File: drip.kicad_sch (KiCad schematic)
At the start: 96 parts, among them J1 ISP, J2 2xAA Battery Holder, Q1 2n2907, Q2 2n2907, Q3 2n2907, Q4 2n2907, Q5 2n2907, Q6 2n2907, Q7 2n2907, Q8 2n2907, Q9 2n2222, SW1 Bin, SW10 Recall, SW11 D, SW12 A, SW13 7, SW14 4, SW15 1, SW16 0, SW17 Hex, SW18 E, SW19 B, SW2 Store, SW20 8, SW21 5, SW22 2, SW23 Decimal, SW24 Oct, SW25 F, SW26 C, SW27 9, SW28 6, SW29 3, SW3 Shift, SW30 +/-, SW31 Clear, SW32 K, SW33 Div, SW34 Mul, SW35 Minus, SW36 Plus, SW37 Enter, SW4 1'sCompl, SW5 Or, SW6 And, SW7 Xor, SW8 Clear Entry, SW9 Dec, U1 74HC138, U2 5641AS-4Digit-7Segment, U3 5641AS-4Digit-7Segment, U4 MSP430G2553IN20, U5 74HC251, U6 74HC138, U7 74HC595, U8 XC6372A331PR-G

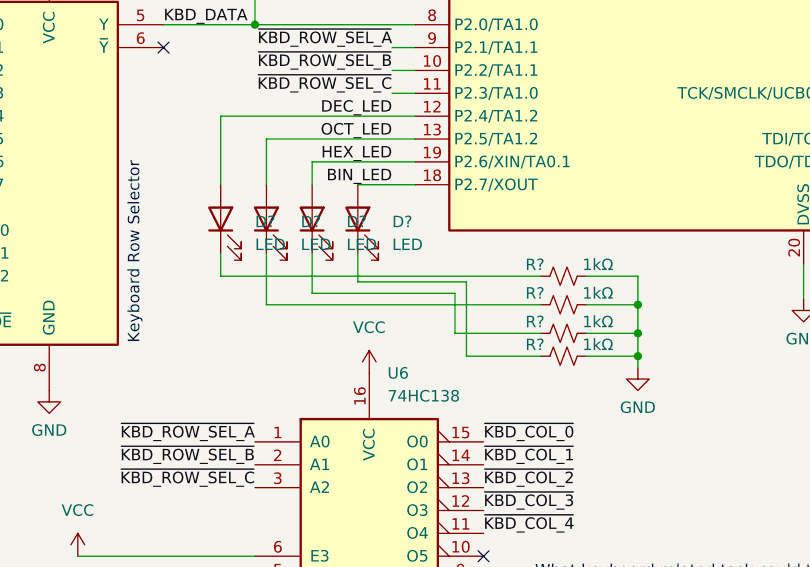
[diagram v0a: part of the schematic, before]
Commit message: Mode LEDs
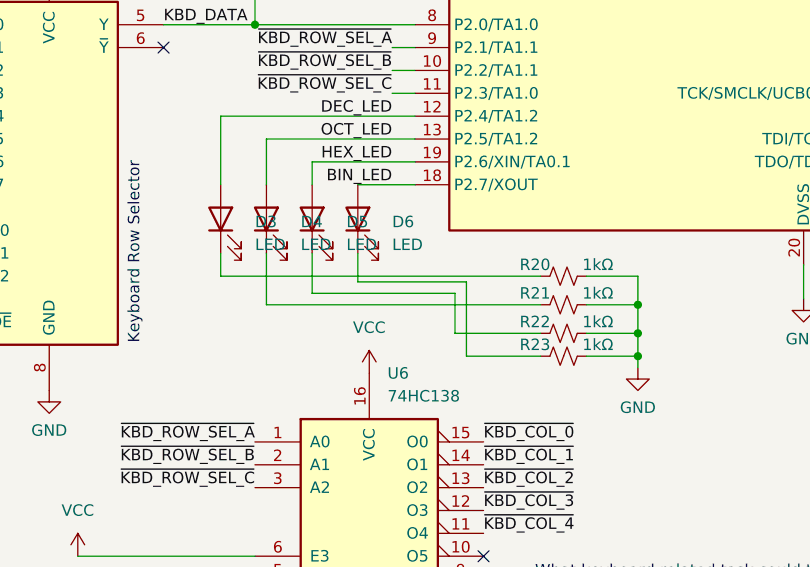
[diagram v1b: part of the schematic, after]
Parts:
- gave numbers to parts that had none: 8
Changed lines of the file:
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@@
   (symbol (lib_id "Device:LED") (at 135.89 203.835 90) (unit 1)
     (in_bom yes) (on_board yes) (fields_autoplaced)
-    (property "Reference" "D?" (id 0) (at 139.7 204.1524 90)
+    (property "Reference" "D4" (id 0) (at 139.7 204.1524 90)
       (effects (font (size 1.27 1.27)) (justify right))
     )
@@
   (symbol (lib_id "Device:R_Small_US") (at 168.91 216.535 90) (unit 1)
     (in_bom yes) (on_board yes)
-    (property "Reference" "R?" (id 0) (at 165.735 215.265 90))
+    (property "Reference" "R22" (id 0) (at 165.735 215.265 90))
     (property "Value" "1kΩ" (id 1) (at 172.72 215.265 90))
     (property "Footprint" "Resistor_SMD:R_0805_2012Metric_Pad1.20x1.40mm_HandSolder" (id 2) (at 168.91 216.535 0)
@@
   (symbol (lib_id "Device:LED") (at 140.97 203.835 90) (unit 1)
     (in_bom yes) (on_board yes) (fields_autoplaced)
-    (property "Reference" "D?" (id 0) (at 144.78 204.1524 90)
+    (property "Reference" "D5" (id 0) (at 144.78 204.1524 90)
       (effects (font (size 1.27 1.27)) (justify right))
     )
@@
   (symbol (lib_id "power:GND") (at 177.165 220.345 0) (unit 1)
     (in_bom yes) (on_board yes) (fields_autoplaced)
-    (property "Reference" "#PWR?" (id 0) (at 177.165 226.695 0)
+    (property "Reference" "#PWR0121" (id 0) (at 177.165 226.695 0)
       (effects (font (size 1.27 1.27)) hide)
     )
@@
   (symbol (lib_id "Device:R_Small_US") (at 168.91 219.075 90) (unit 1)
     (in_bom yes) (on_board yes)
-    (property "Reference" "R?" (id 0) (at 165.735 217.805 90))
+    (property "Reference" "R23" (id 0) (at 165.735 217.805 90))
     (property "Value" "1kΩ" (id 1) (at 172.72 217.805 90))
     (property "Footprint" "Resistor_SMD:R_0805_2012Metric_Pad1.20x1.40mm_HandSolder" (id 2) (at 168.91 219.075 0)
@@
   (symbol (lib_id "Device:LED") (at 146.05 203.835 90) (unit 1)
     (in_bom yes) (on_board yes) (fields_autoplaced)
-    (property "Reference" "D?" (id 0) (at 149.86 204.1524 90)
+    (property "Reference" "D6" (id 0) (at 149.86 204.1524 90)
       (effects (font (size 1.27 1.27)) (justify right))
     )
@@
   (symbol (lib_id "Device:R_Small_US") (at 168.91 210.185 90) (unit 1)
     (in_bom yes) (on_board yes)
-    (property "Reference" "R?" (id 0) (at 165.735 208.915 90))
+    (property "Reference" "R20" (id 0) (at 165.735 208.915 90))
     (property "Value" "1kΩ" (id 1) (at 172.72 208.915 90))
     (property "Footprint" "Resistor_SMD:R_0805_2012Metric_Pad1.20x1.40mm_HandSolder" (id 2) (at 168.91 210.185 0)
@@
   (symbol (lib_id "Device:LED") (at 130.81 203.835 90) (unit 1)
     (in_bom yes) (on_board yes) (fields_autoplaced)
-    (property "Reference" "D?" (id 0) (at 134.62 204.1524 90)
+    (property "Reference" "D3" (id 0) (at 134.62 204.1524 90)
       (effects (font (size 1.27 1.27)) (justify right))
     )
@@
   (symbol (lib_id "Device:R_Small_US") (at 168.91 213.36 90) (unit 1)
     (in_bom yes) (on_board yes)
-    (property "Reference" "R?" (id 0) (at 165.735 212.09 90))
+    (property "Reference" "R21" (id 0) (at 165.735 212.09 90))
     (property "Value" "1kΩ" (id 1) (at 172.72 212.09 90))
     (property "Footprint" "Resistor_SMD:R_0805_2012Metric_Pad1.20x1.40mm_HandSolder" (id 2) (at 168.91 213.36 0)
@@
     )
     (path "/673b1f10-dd13-4373-9e76-ed62eba7cac1"
-      (reference "#PWR?") (unit 1) (value "GND") (footprint "")
+      (reference "#PWR0121") (unit 1) (value "GND") (footprint "")
     )
     (path "/f2caa468-bb79-49cc-b0cf-a4c553ec891c"
@@
       (reference "D2") (unit 1) (value "1n5817") (footprint "Diode_THT:D_DO-41_SOD81_P10.16mm_Horizontal")
     )
+    (path "/be978f47-2533-42ed-ab73-ed75e74230d9"
+      (reference "D3") (unit 1) (value "LED") (footprint "LED_SMD:LED_0805_2012Metric_Pad1.15x1.40mm_HandSolder")
+    )
     (path "/22a290e3-58c4-4aae-b185-93fd6b844074"
-      (reference "D?") (unit 1) (value "LED") (footprint "LED_SMD:LED_0805_2012Metric_Pad1.15x1.40mm_HandSolder")
+      (reference "D4") (unit 1) (value "LED") (footprint "LED_SMD:LED_0805_2012Metric_Pad1.15x1.40mm_HandSolder")
     )
     (path "/5943c4e7-6e09-4c4b-8a82-3e90b1f52c8c"
-      (reference "D?") (unit 1) (value "LED") (footprint "LED_SMD:LED_0805_2012Metric_Pad1.15x1.40mm_HandSolder")
+      (reference "D5") (unit 1) (value "LED") (footprint "LED_SMD:LED_0805_2012Metric_Pad1.15x1.40mm_HandSolder")
     )
     (path "/80b2e35d-fdef-444f-8ff8-9f92d6753b6a"
-      (reference "D?") (unit 1) (value "LED") (footprint "LED_SMD:LED_0805_2012Metric_Pad1.15x1.40mm_HandSolder")
-    )
-    (path "/be978f47-2533-42ed-ab73-ed75e74230d9"
-      (reference "D?") (unit 1) (value "LED") (footprint "LED_SMD:LED_0805_2012Metric_Pad1.15x1.40mm_HandSolder")
+      (reference "D6") (unit 1) (value "LED") (footprint "LED_SMD:LED_0805_2012Metric_Pad1.15x1.40mm_HandSolder")
     )
     (path "/1316d982-f638-40c6-90fd-9cab7a83850f"
@@
       (reference "R19") (unit 1) (value "10kΩ") (footprint "Resistor_THT:R_Axial_DIN0207_L6.3mm_D2.5mm_P10.16mm_Horizontal")
     )
+    (path "/82c4e075-27e8-41a6-926f-b8b505d03e9f"
+      (reference "R20") (unit 1) (value "1kΩ") (footprint "Resistor_SMD:R_0805_2012Metric_Pad1.20x1.40mm_HandSolder")
+    )
+    (path "/f1a1bee2-b923-440b-afe1-25c56dc0de35"
+      (reference "R21") (unit 1) (value "1kΩ") (footprint "Resistor_SMD:R_0805_2012Metric_Pad1.20x1.40mm_HandSolder")
+    )
     (path "/40a8bdb3-621f-4c90-883d-072d466d3a70"
-      (reference "R?") (unit 1) (value "1kΩ") (footprint "Resistor_SMD:R_0805_2012Metric_Pad1.20x1.40mm_HandSolder")
+      (reference "R22") (unit 1) (value "1kΩ") (footprint "Resistor_SMD:R_0805_2012Metric_Pad1.20x1.40mm_HandSolder")
     )
     (path "/7c7e3dd1-1cf4-4260-96bf-0365fab23f81"
-      (reference "R?") (unit 1) (value "1kΩ") (footprint "Resistor_SMD:R_0805_2012Metric_Pad1.20x1.40mm_HandSolder")
-    )
-    (path "/82c4e075-27e8-41a6-926f-b8b505d03e9f"
-      (reference "R?") (unit 1) (value "1kΩ") (footprint "Resistor_SMD:R_0805_2012Metric_Pad1.20x1.40mm_HandSolder")
-    )
-    (path "/f1a1bee2-b923-440b-afe1-25c56dc0de35"
-      (reference "R?") (unit 1) (value "1kΩ") (footprint "Resistor_SMD:R_0805_2012Metric_Pad1.20x1.40mm_HandSolder")
+      (reference "R23") (unit 1) (value "1kΩ") (footprint "Resistor_SMD:R_0805_2012Metric_Pad1.20x1.40mm_HandSolder")
     )
     (path "/f2abe8e1-ca83-4046-8fbf-377cee622491"

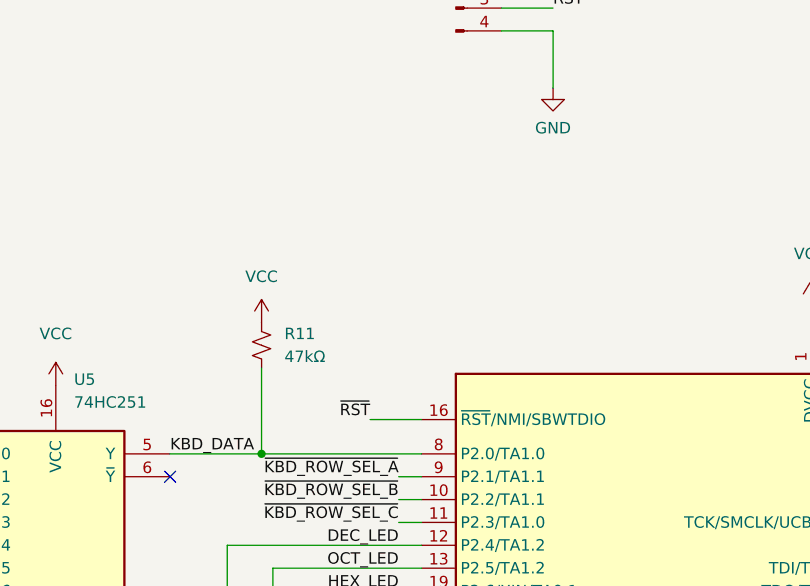
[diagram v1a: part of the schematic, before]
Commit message: Reset pullup, move test hooks further apart
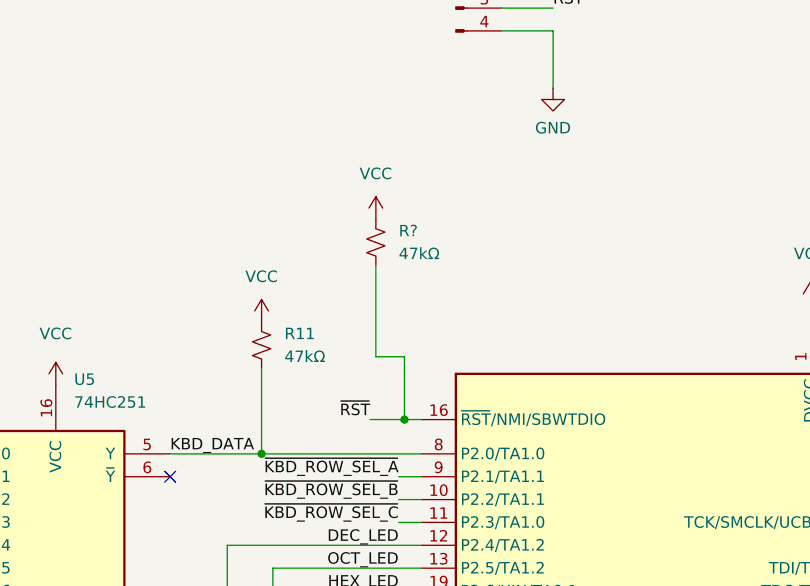
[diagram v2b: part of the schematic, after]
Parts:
- added R?: 47kΩ, Resistor_THT:R_Axial_DIN0207_L6.3mm_D2.5mm_P10.16mm_Horizontal, symbol Device:R_Small_US
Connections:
- net VCC: now also R?.1
- net ~{RST}: now also R?.2
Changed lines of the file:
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@@
   (junction (at 92.71 295.275) (diameter 0) (color 0 0 0 0)
   )
+  (junction (at 150.495 178.435) (diameter 0) (color 0 0 0 0)
+  )
   (junction (at 73.025 313.055) (diameter 0) (color 0 0 0 0)
   )
@@
     (stroke (width 0) (type default) (color 0 0 0 0))
   )
+  (wire (pts (xy 147.32 171.45) (xy 150.495 171.45))
+    (stroke (width 0) (type default) (color 0 0 0 0))
+  )
   (wire (pts (xy 117.475 62.23) (xy 117.475 72.39))
     (stroke (width 0) (type default) (color 0 0 0 0))
@@
     (stroke (width 0) (type default) (color 0 0 0 0))
   )
+  (wire (pts (xy 150.495 171.45) (xy 150.495 178.435))
+    (stroke (width 0) (type default) (color 0 0 0 0))
+  )
   (wire (pts (xy 318.77 296.545) (xy 323.215 296.545))
     (stroke (width 0) (type default) (color 0 0 0 0))
@@
     (stroke (width 0) (type default) (color 0 0 0 0))
   )
-  (wire (pts (xy 146.685 178.435) (xy 152.4 178.435))
+  (wire (pts (xy 146.685 178.435) (xy 150.495 178.435))
     (stroke (width 0) (type default) (color 0 0 0 0))
   )
@@
     (stroke (width 0) (type default) (color 0 0 0 0))
   )
+  (wire (pts (xy 150.495 178.435) (xy 152.4 178.435))
+    (stroke (width 0) (type default) (color 0 0 0 0))
+  )
   (wire (pts (xy 375.92 271.78) (xy 375.92 261.62))
     (stroke (width 0) (type default) (color 0 0 0 0))
@@
     (stroke (width 0) (type default) (color 0 0 0 0))
   )
+  (wire (pts (xy 147.32 161.29) (xy 147.32 171.45))
+    (stroke (width 0) (type default) (color 0 0 0 0))
+  )
   (wire (pts (xy 161.29 132.715) (xy 167.005 132.715))
     (stroke (width 0) (type default) (color 0 0 0 0))
@@
     (pin "2")
   )
+  (symbol (lib_id "power:VCC") (at 147.32 156.21 0) (unit 1)
+    (in_bom yes) (on_board yes) (fields_autoplaced)
+    (property "Reference" "#PWR?" (id 0) (at 147.32 160.02 0)
+      (effects (font (size 1.27 1.27)) hide)
+    )
+    (property "Value" "VCC" (id 1) (at 147.32 151.13 0))
+    (property "Footprint" "" (id 2) (at 147.32 156.21 0)
+      (effects (font (size 1.27 1.27)) hide)
+    )
+    (property "Datasheet" "" (id 3) (at 147.32 156.21 0)
+      (effects (font (size 1.27 1.27)) hide)
+    )
+    (pin "1")
+  )
   (symbol (lib_id "Jumper:Jumper_2_Bridged") (at 335.28 351.79 0) (unit 1)
     (in_bom yes) (on_board yes) (fields_autoplaced)
@@
     (pin "1")
   )
+  (symbol (lib_id "Device:R_Small_US") (at 147.32 158.75 0) (unit 1)
+    (in_bom yes) (on_board yes) (fields_autoplaced)
+    (property "Reference" "R?" (id 0) (at 149.86 157.4799 0)
+      (effects (font (size 1.27 1.27)) (justify left))
+    )
+    (property "Value" "47kΩ" (id 1) (at 149.86 160.0199 0)
+      (effects (font (size 1.27 1.27)) (justify left))
+    )
+    (property "Footprint" "Resistor_THT:R_Axial_DIN0207_L6.3mm_D2.5mm_P10.16mm_Horizontal" (id 2) (at 147.32 158.75 0)
+      (effects (font (size 1.27 1.27)) hide)
+    )
+    (property "Datasheet" "~" (id 3) (at 147.32 158.75 0)
+      (effects (font (size 1.27 1.27)) hide)
+    )
+    (pin "1")
+    (pin "2")
+  )
   (symbol (lib_id "Device:R_Small_US") (at 393.065 346.71 90) (unit 1)
     (in_bom yes) (on_board yes)
@@
       (reference "#PWR0121") (unit 1) (value "GND") (footprint "")
     )
+    (path "/5fe5395c-78d6-40cf-b4c7-813897577b4a"
+      (reference "#PWR?") (unit 1) (value "VCC") (footprint "")
+    )
     (path "/f2caa468-bb79-49cc-b0cf-a4c553ec891c"
       (reference "C1") (unit 1) (value "220µF") (footprint "Capacitor_THT:CP_Radial_D8.0mm_P5.00mm")
@@
       (reference "R23") (unit 1) (value "1kΩ") (footprint "Resistor_SMD:R_0805_2012Metric_Pad1.20x1.40mm_HandSolder")
     )
+    (path "/c89464ff-21e6-4876-b3fa-6ec0b5c531f1"
+      (reference "R?") (unit 1) (value "47kΩ") (footprint "Resistor_THT:R_Axial_DIN0207_L6.3mm_D2.5mm_P10.16mm_Horizontal")
+    )
     (path "/f2abe8e1-ca83-4046-8fbf-377cee622491"
